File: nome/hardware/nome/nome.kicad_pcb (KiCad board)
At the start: 2 copper layers, 91.4 x 91.4 mm, 64 parts, among them J1 SJ-2524, J2 JTAG_SWD, J3 JST, J4 7SEG_DEBUG, SW1 SW_SPDT, SW2 Rotary_Encoder_Switch, U1 LM1117-1.8, U2 LM1117-3.3, U3 AS1115, U4 STMF411CEU6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

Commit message: Add speaker polarity labels
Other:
- board text added: "+"
- board text added: "-"
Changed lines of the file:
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@@
 (general
   (thickness 1.6)
-  (drawings 10)
+  (drawings 12)
   (tracks 937)
   (zones 0)
@@
     )
   )
+  (gr_text - (at 58.42 53.34) (layer F.SilkS)
+    (effects (font (size 1.5 1.5) (thickness 0.3)))
+  )
+  (gr_text + (at 53.34 53.34) (layer F.SilkS)
+    (effects (font (size 1.5 1.5) (thickness 0.3)))
+  )
   (gr_text "rev. A" (at 36.068 60.452) (layer F.SilkS)

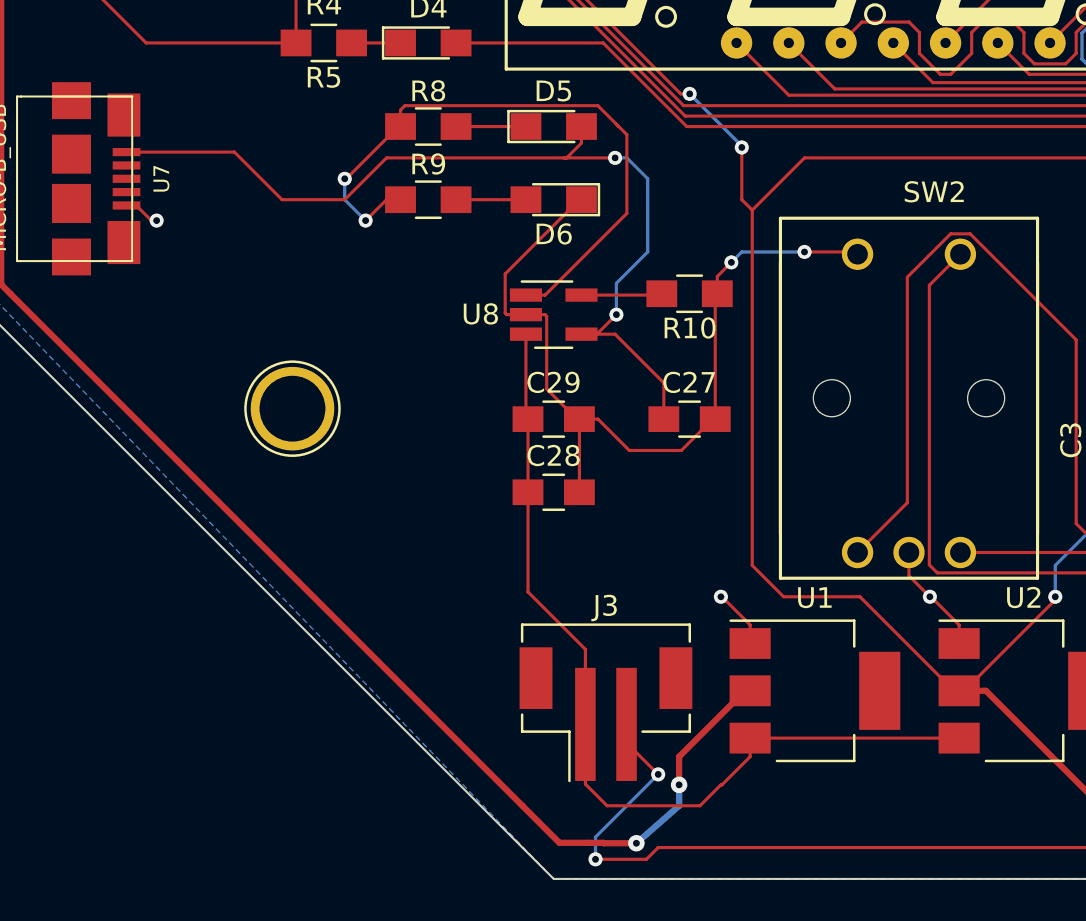
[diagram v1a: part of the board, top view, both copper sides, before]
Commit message: Widen some more power rails
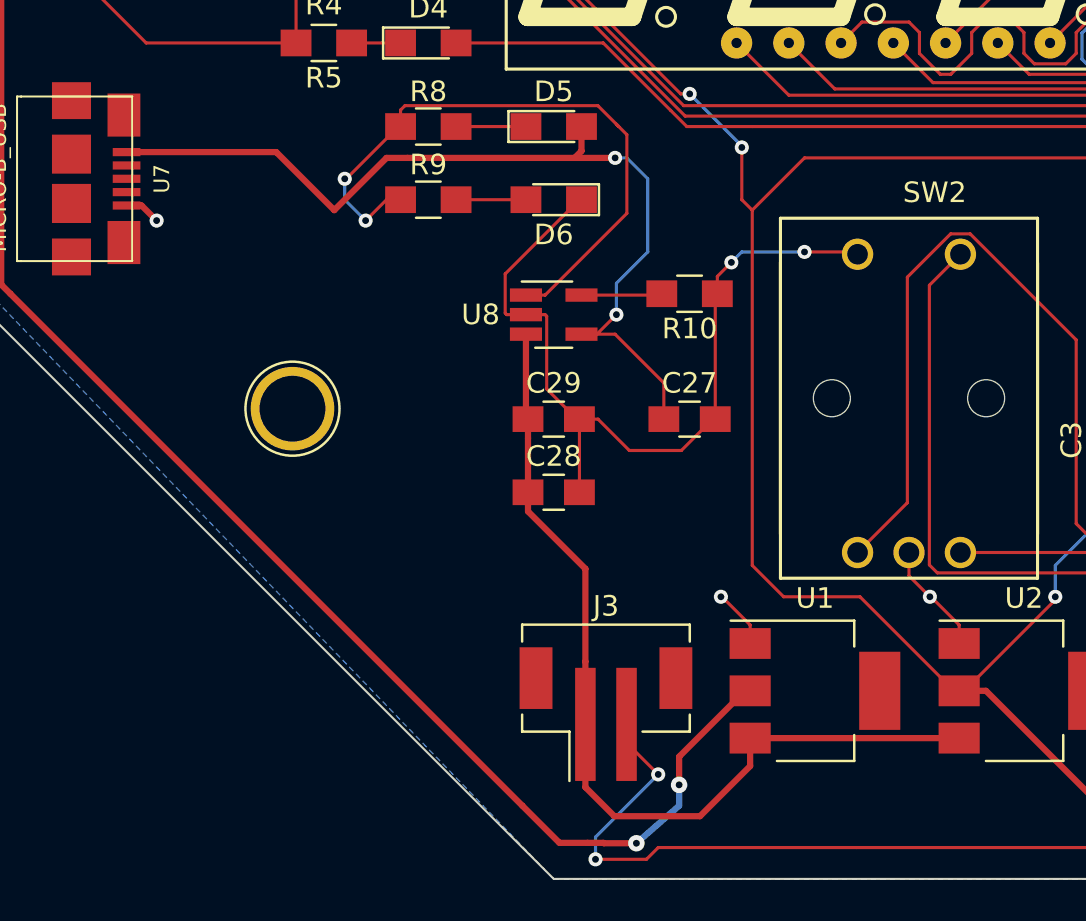
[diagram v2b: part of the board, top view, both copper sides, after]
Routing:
- net Net-(C28-Pad1): track 43.6 -> 44.3 mm
- net Net-(C27-Pad1): track 45.6 -> 46.4 mm
- net GND: track 260.3 -> 261.0 mm
